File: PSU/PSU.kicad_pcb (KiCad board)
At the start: 2 copper layers, 226.1 x 106.7 mm, 54 parts, among them J1 Screw_Terminal_01x02, J2 Screw_Terminal_01x02, J3 Screw_Terminal_01x02, U1 STPS10L25G-TR, U2 STPS10L25G-TR, U3 L4975A, U4 STPS10L25G-TR, U5 STPS10L25G-TR, U6 L4975A

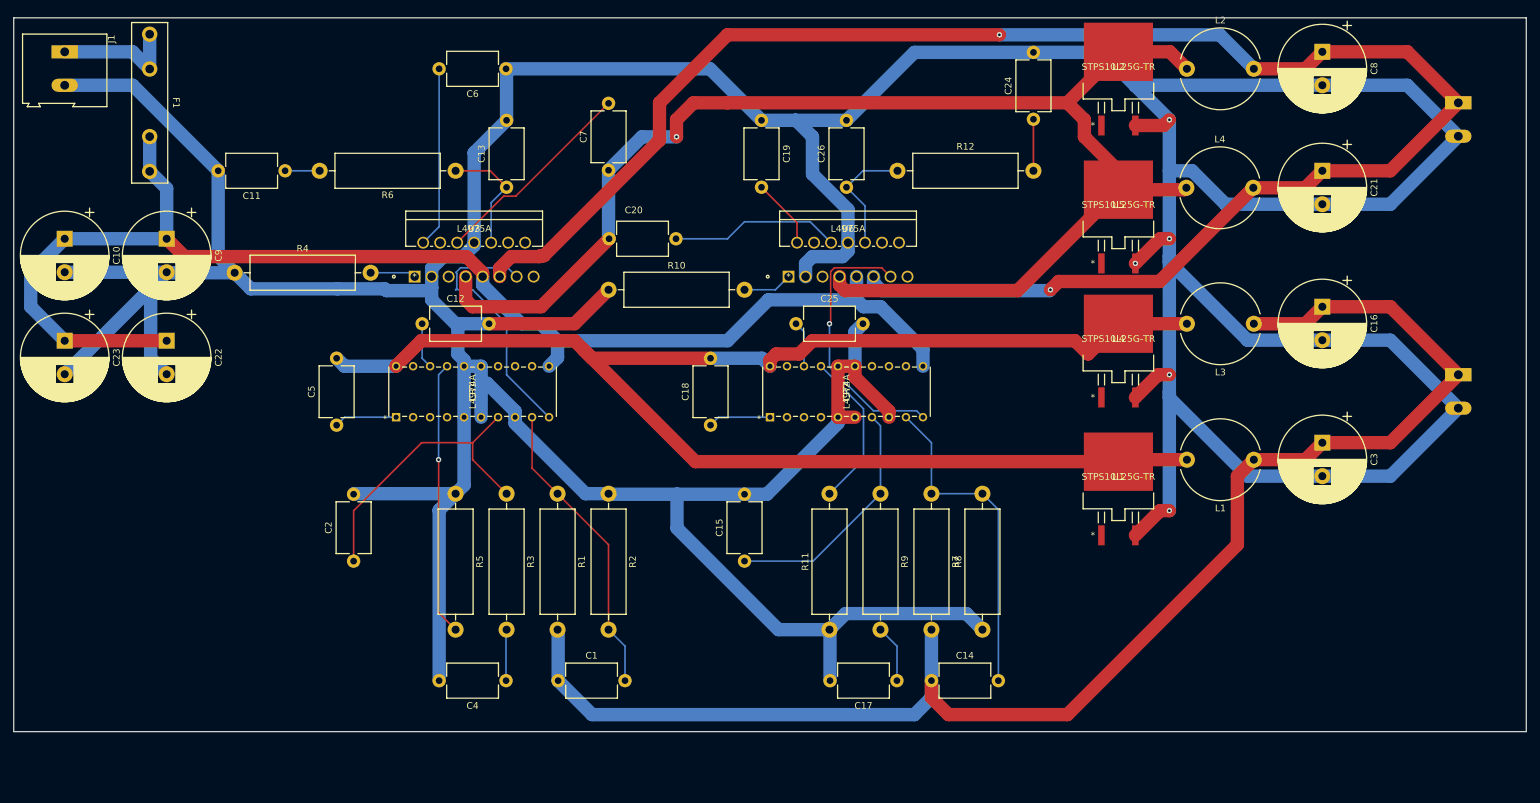
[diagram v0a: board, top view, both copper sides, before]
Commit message: Revisited PCB
- SMT resistors instead of THT
- Added LEDs
- Added emergency stop button connector
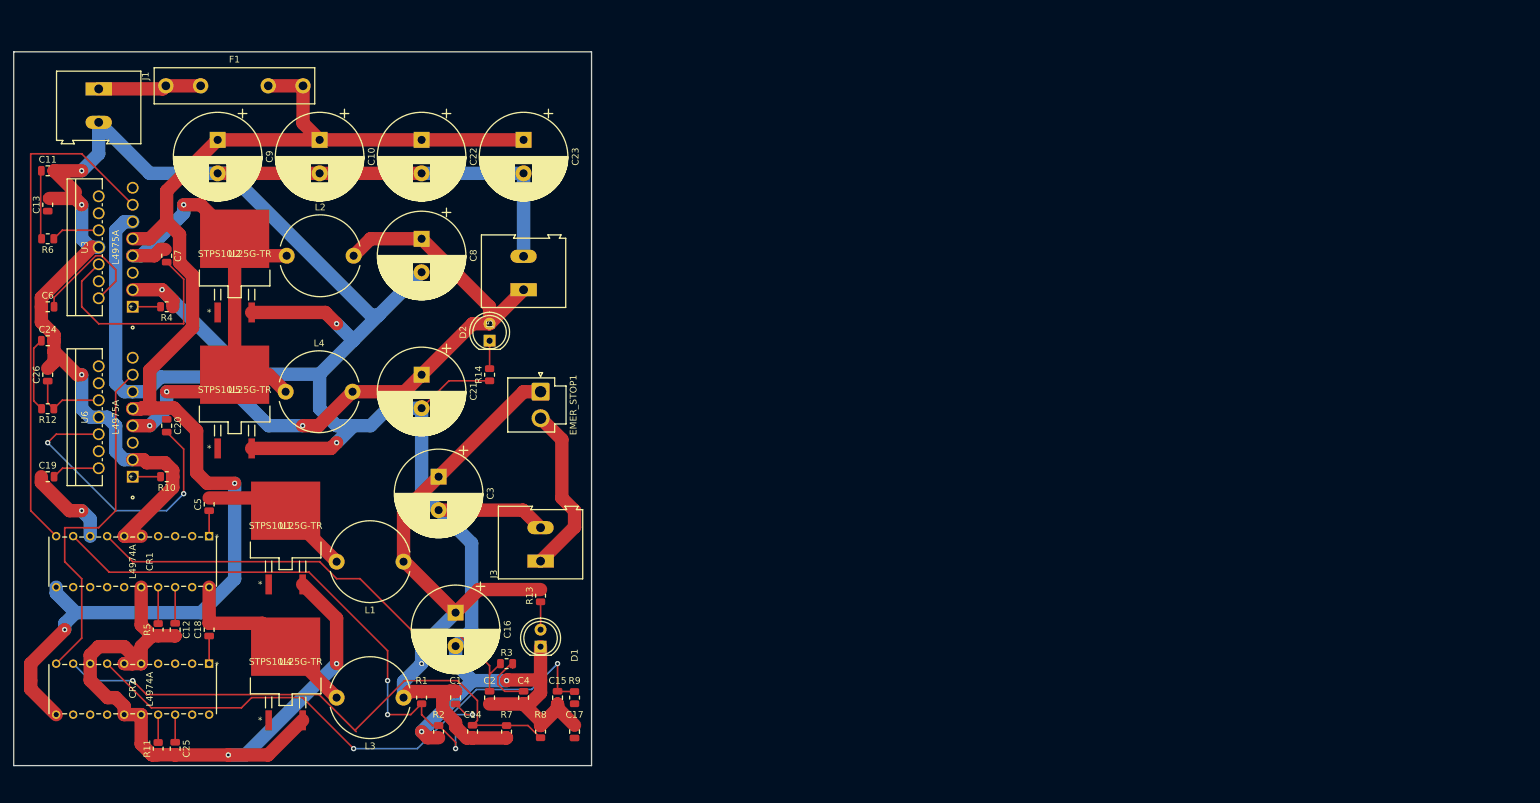
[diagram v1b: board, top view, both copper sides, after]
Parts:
- removed J2: Screw_Terminal_01x02, TerminalBlock:TerminalBlock_Altech_AK300-2_P5.00mm
- added D1: LED, LED_THT:LED_D5.0mm, F.Cu at (91.4, 106.7)
- added D2: LED, LED_THT:LED_D5.0mm, F.Cu at (83.8, 61.0)
- added EMER_STOP1: Conn_01x02_Male, Connector_JST:JST_VH_B2P-VH-B_1x02_P3.96mm_Vertical, F.Cu at (91.4, 68.6)
- added J5: 5VOUT, TerminalBlock:TerminalBlock_Altech_AK300-2_P5.00mm, F.Cu at (88.9, 53.3)
- added R13: 500, Resistor_SMD:R_0805_2012Metric, F.Cu at (91.4, 99.1)
- added R14: 150, Resistor_SMD:R_0805_2012Metric, F.Cu at (83.8, 66.0)
- C1, C11, C12, C13, C14, C15, C17, C18, C19, C2, C20, C24, C25, C26, C4, C5, C6, C7: footprint Capacitor_THT:C_Disc_D7.5mm_W5.0mm_P10.00mm -> Capacitor_SMD:C_0805_2012Metric
- J1: value Screw_Terminal_01x02 -> VBATIN
- J3: value Screw_Terminal_01x02 -> 12VOUT; moved to F.Cu
- R1, R10, R11, R12, R2, R3, R4, R5, R6, R7, R8, R9: footprint Resistor_THT:R_Axial_DIN0516_L15.5mm_D5.0mm_P20.32mm_Horizontal -> Resistor_SMD:R_0805_2012Metric
- moved C24 151.0 mm to (17.8, 61.0), turned to 0 degrees
- moved J3 140.0 mm to (91.4, 93.9), turned to 90 degrees
- moved L3 138.8 mm to (71.0, 114.3)
- moved C21 138.0 mm to (73.7, 66.0)
- moved L4 138.0 mm to (53.3, 68.6)
- moved C8 137.5 mm to (73.7, 45.7)
- moved L2 137.4 mm to (53.5, 48.3)
- moved C16 137.4 mm to (78.7, 101.6)
- moved U2 135.0 mm to (45.7, 48.0)
- moved U5 134.9 mm to (45.7, 68.3)
- moved U4 133.5 mm to (53.3, 108.9)
- moved C3 132.2 mm to (76.2, 81.3)
- moved R12 131.9 mm to (17.8, 71.1), turned to 180 degrees
- moved L1 128.0 mm to (71.0, 94.0)
- moved U1 124.7 mm to (53.3, 88.6)
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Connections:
- net 5VOUT renamed +5V
- net VBATFUS renamed +24V
- C1 pad 1: 12VOUT -> +12V
- C14 pad 1: 12VOUT -> +12V
- C16 pad 1: 12VOUT -> +12V
- C3 pad 1: 12VOUT -> +12V
- J3 pad 1: 12VOUT -> /12VOUTPOSTEMER
- L1 pad 1: 12VOUT -> +12V
- L3 pad 1: 12VOUT -> +12V
- R1 pad 2: 12VOUT -> +12V
- R7 pad 2: 12VOUT -> +12V
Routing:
- net GND: track 887.0 -> 576.7 mm, vias 5 -> 11
- net 12VOUT: track 222.0 -> 0.00 mm
- net /12VOUTPREIND: track 232.9 -> 52.0 mm
- net +5V: track 269.0 -> 127.9 mm, vias 2 -> 1
- net /5VOUTPREIND: track 212.1 -> 84.1 mm, vias 1 -> 3
- net +12V: track 0.00 -> 100.5 mm, vias 0 -> 1
- net Net-(C15-Pad1): track 36.5 -> 85.8 mm, vias 0 -> 2
- net Net-(C1-Pad2): track 45.1 -> 89.6 mm, vias 0 -> 4
- net Net-(CR1-Pad10): track 39.0 -> 77.1 mm
- net Net-(CR1-Pad17): track 40.9 -> 5.44 mm, vias 1 -> 0
- net Net-(C14-Pad2): track 49.6 -> 84.1 mm, vias 0 -> 1
- net Net-(C2-Pad1): track 44.6 -> 71.3 mm
- net /12VOUTPOSTEMER: track 0.00 -> 25.6 mm
- net Net-(CR2-Pad17): track 23.8 -> 4.17 mm
- net Net-(C20-Pad2): track 25.5 -> 44.0 mm, vias 0 -> 2
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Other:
- board size 226.1 x 106.7 mm -> 86.4 x 106.7 mm
- board text added: "12VOUT"
- board text added: "5VOUT"
- board text added: "EUROBOT PSU - AREM ISMIN 2022"

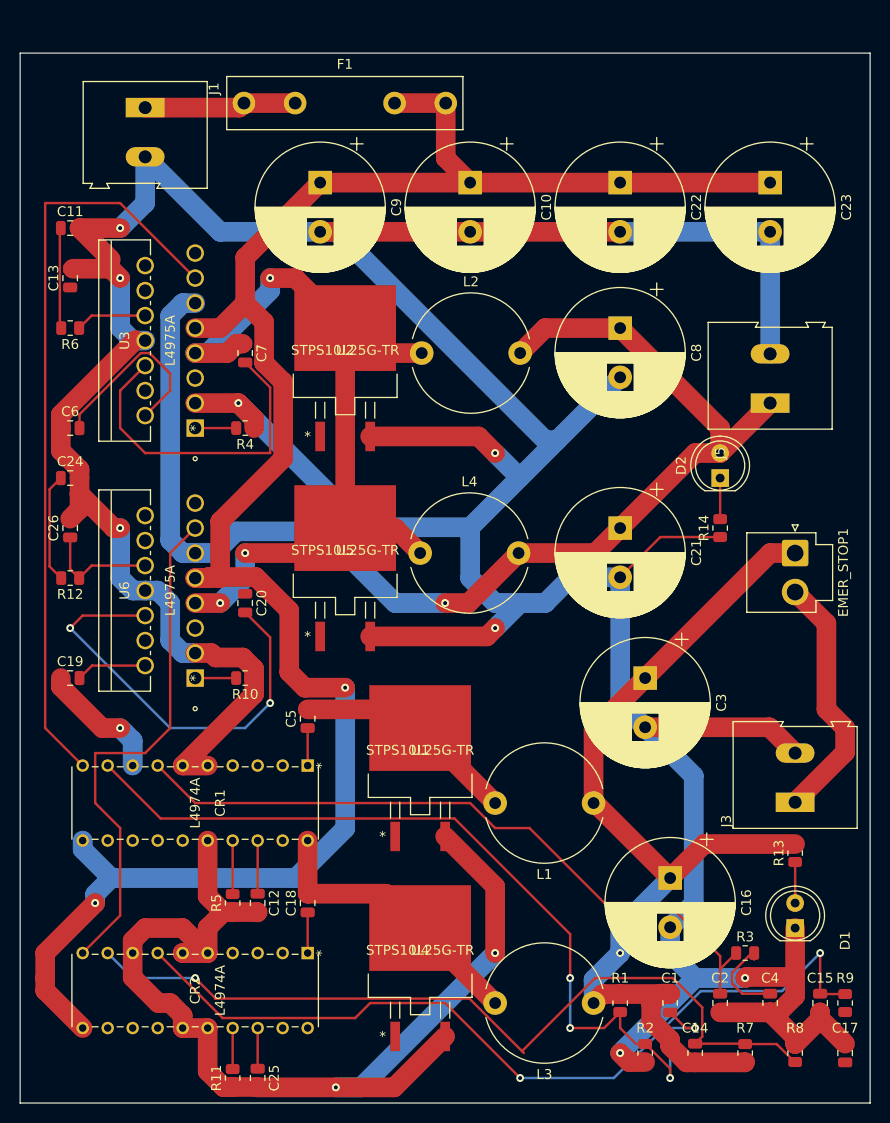
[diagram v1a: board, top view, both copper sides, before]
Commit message: Added switch and made space for inductors
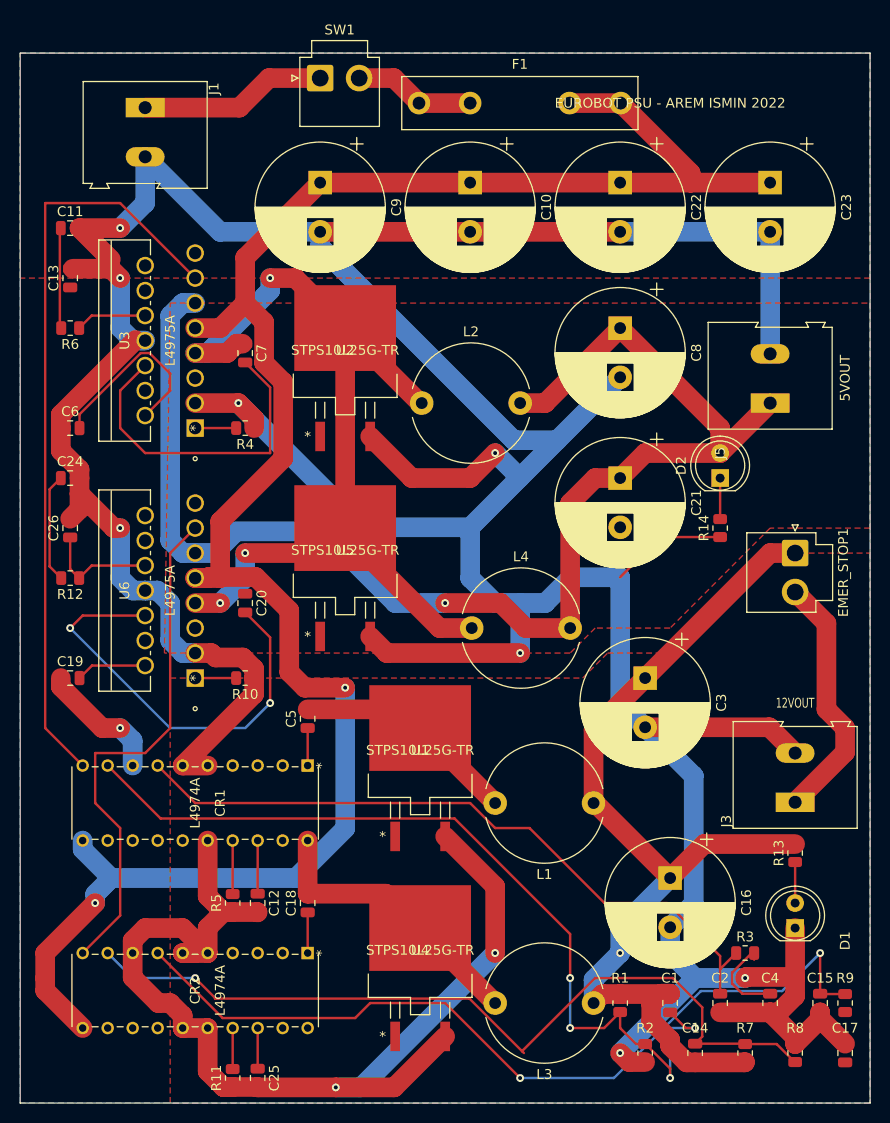
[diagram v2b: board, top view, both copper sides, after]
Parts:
- added SW1: SW_SPST, Connector_JST:JST_VH_B2P-VH_1x02_P3.96mm_Vertical, F.Cu at (43.2, 20.3)
- moved F1 17.8 mm to (53.2, 22.9)
- moved L4 9.25 mm to (58.6, 76.2)
- moved C21 5.08 mm to (73.7, 61.0)
- moved L2 5.08 mm to (53.5, 53.3)
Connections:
- F1 pad 1: /VBAT -> /VBATPOSTSWITCH
- J1 pad 1: /VBAT -> /VBATPRESWITCH
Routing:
- net /VBATPRESWITCH: track 0.00 -> 19.0 mm
- net /VBAT: track 15.4 -> 0.00 mm
- net /VBATPOSTSWITCH: track 0.00 -> 12.3 mm
- net +5V: track 127.9 -> 139.5 mm
- net /5VOUTPREIND: track 84.1 -> 95.0 mm
- net GND: track 576.7 -> 584.1 mm
- net +24V: track 204.7 -> 206.6 mm
- added copper zone on F.Cu, net +12V
- added copper zone on F.Cu, net +24V
- added copper zone on F.Cu, net +5V
- added copper zone on B.Cu, net GND

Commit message: Final layout
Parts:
- added H2: MountingHole, MountingHole:MountingHole_3.2mm_M3, F.Cu at (91.4, 22.9)
- added H3: MountingHole, MountingHole:MountingHole_3.2mm_M3, F.Cu at (17.8, 121.9)
- added H4: MountingHole, MountingHole:MountingHole_3.2mm_M3, F.Cu at (17.8, 22.9)
- added H5: MountingHole, MountingHole:MountingHole_3.2mm_M3, F.Cu at (91.4, 121.9)
- C8: value 1000uF -> 3300uF
- moved L3 7.07 mm to (66.0, 119.4), turned to 90 degrees
- moved C20 2.54 mm to (35.6, 76.2)
- moved J1 2.54 mm to (27.9, 23.3)
- moved R8 2.54 mm to (91.4, 116.8)
- moved L4 0.08 mm to (58.5, 76.2), turned to 90 degrees
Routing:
- net /12VOUTPREIND: track 52.0 -> 94.5 mm, vias 0 -> 2
- net GND: track 584.1 -> 597.0 mm
- net +12V: track 100.5 -> 109.1 mm, vias 1 -> 2
- net +5V: track 139.5 -> 148.1 mm
- net Net-(C17-Pad1): track 0.00 -> 8.05 mm
- net Net-(C13-Pad1): track 7.23 -> 11.7 mm
- net /5VOUTPREIND: track 95.0 -> 98.2 mm
- net Net-(C20-Pad2): track 44.0 -> 41.4 mm
- net /VBATPRESWITCH: track 19.0 -> 16.5 mm
- net Net-(C15-Pad1): track 85.8 -> 84.5 mm
- added copper zone on F.Cu, net /12VOUTPOSTEMER
- added copper zone on F.Cu, net /12VOUTPREIND
- added copper zone on F.Cu, net /5VOUTPREIND
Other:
- board size 86.4 x 106.7 mm -> 86.4 x 109.2 mm
